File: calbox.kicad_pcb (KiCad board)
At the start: 2 copper layers, 101.6 x 76.2 mm, 80 parts, among them P1 BNC, P2 BAN+, P3 BAN-, Q1 MMBT2369, SW1 ROTARY 7POS, SW2 ROTARY 3POS, SW3 SPDT, SW4 ROTARY 12POS, SW5 DPST, U1 74LVC161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

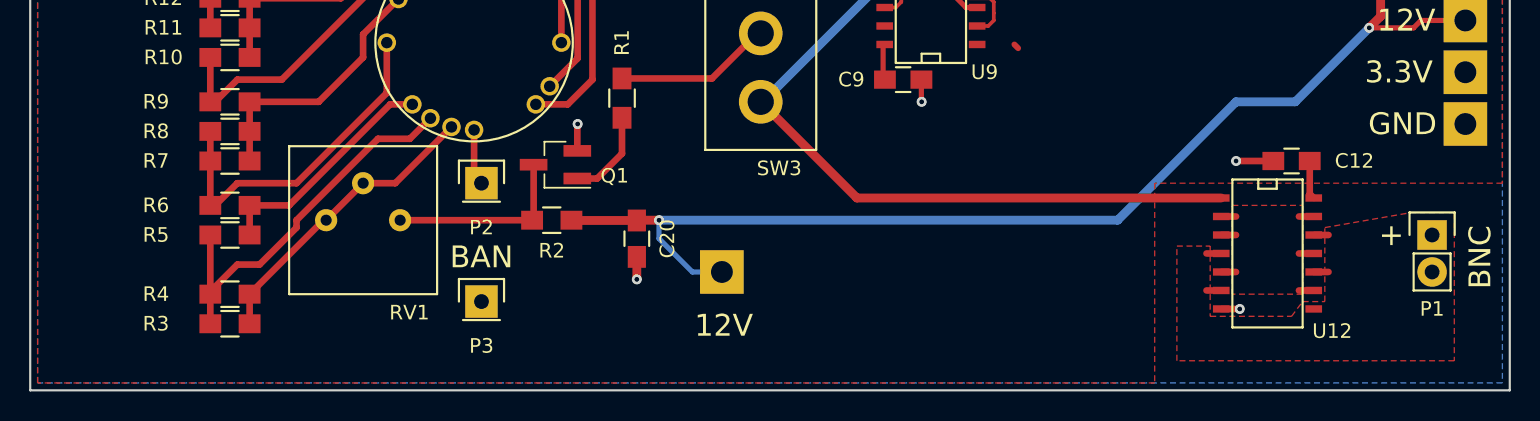
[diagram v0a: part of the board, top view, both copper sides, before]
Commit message: updated layout, specifically banana plug attachment points
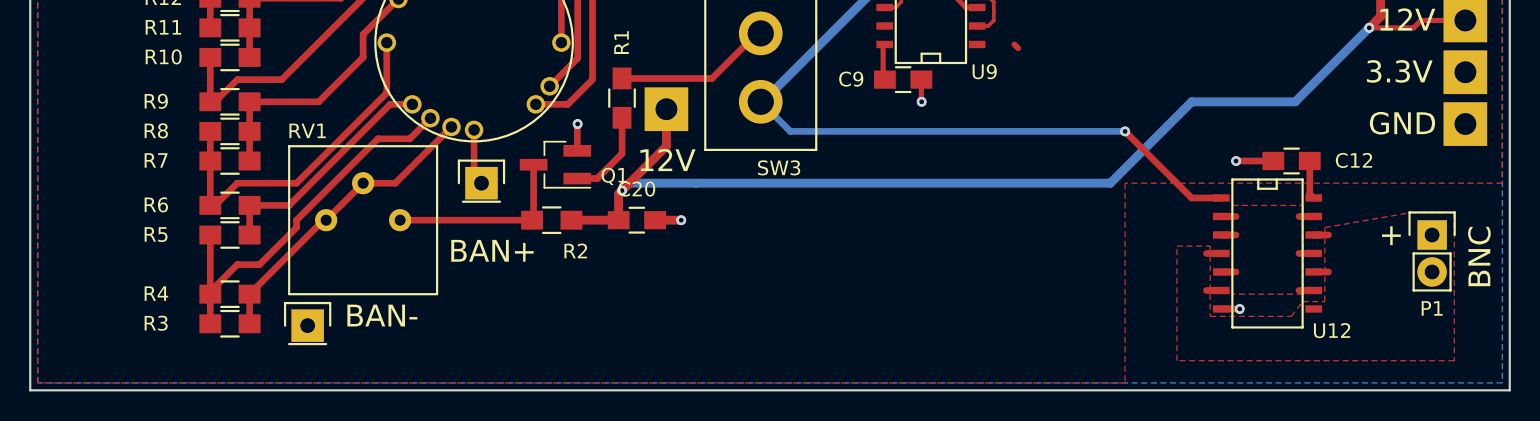
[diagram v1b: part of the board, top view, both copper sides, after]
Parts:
- moved P3 12.1 mm to (85.1, 158.1)
- moved TP1 11.8 mm to (109.7, 143.3)
- moved C20 1.27 mm to (107.7, 150.9), turned to 0 degrees
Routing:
- net +12V: track 132.9 -> 134.3 mm
- net /clock_final_division/clock_final_division_out: vias 0 -> 1
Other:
- board text added: "BAN+"
- board text added: "BAN-"
- board text removed: "BAN"

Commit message: version sent to EasyEDA 3/26/17
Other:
- board text added: "calbox Graham Keeth 3/2017"
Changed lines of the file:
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@@
     (links 255)
     (no_connects 0)
-    (area 65.964999 86.284999 167.715001 162.635001)
+    (area 31.214287 44.036 201.957715 177.96)
     (thickness 1.6)
-    (drawings 30)
-    (tracks 724)
+    (drawings 31)
+    (tracks 726)
     (zones 0)
     (modules 80)
@@
   (layers
     (0 F.Cu signal)
-    (31 B.Cu signal hide)
+    (31 B.Cu signal)
     (33 F.Adhes user)
     (35 F.Paste user)
     (37 F.SilkS user)
+    (38 B.Mask user)
     (39 F.Mask user)
-    (40 Dwgs.User user hide)
-    (41 Cmts.User user hide)
-    (42 Eco1.User user hide)
-    (43 Eco2.User user hide)
+    (40 Dwgs.User user)
+    (41 Cmts.User user)
+    (42 Eco1.User user)
+    (43 Eco2.User user)
     (44 Edge.Cuts user)
     (45 Margin user)
@@
   )
   (setup
-    (last_trace_width 0.6096)
+    (last_trace_width 0.254)
     (user_trace_width 0.3048)
     (user_trace_width 0.3556)
@@
     (visible_elements FFFEFFFF)
     (pcbplotparams
-      (layerselection 0x00030_80000001)
-      (usegerberextensions false)
+      (layerselection 0x29fe0_80000001)
+      (usegerberextensions true)
       (excludeedgelayer true)
       (linewidth 0.100000)
@@
       (plotinvisibletext false)
       (padsonsilk false)
-      (subtractmaskfromsilk false)
+      (subtractmaskfromsilk true)
       (outputformat 1)
       (mirror false)
-      (drillshape 1)
+      (drillshape 0)
       (scaleselection 1)
-      (outputdirectory ""))
+      (outputdirectory fab/gerber))
   )
   (net 0 "")
@@
     (tags "capacitor 0805")
     (attr smd)
-    (fp_text reference C20 (at 0 -2.1) (layer F.SilkS)
+    (fp_text reference C20 (at 0.254 2.159) (layer F.SilkS)
       (effects (font (size 1 1) (thickness 0.15)))
     )
@@
     )
   )
+  (gr_text "calbox\nGraham Keeth\n3/2017" (at 117.475 154.94) (layer F.SilkS)
+    (effects (font (size 1.5 1.5) (thickness 0.3) italic) (justify left))
+  )
   (gr_line (start 167.64 162.56) (end 66.04 162.56) (angle 90) (layer Edge.Cuts) (width 0.15))
   (gr_text BAN- (at 90.17 157.48) (layer F.SilkS)
@@
   (segment (start 131.064 133.731) (end 133.604 133.731) (width 0.4064) (layer F.Cu) (net 42))
   (segment (start 130.175 114.935) (end 128.69868 113.45868) (width 0.4064) (layer F.Cu) (net 42))
+  (segment (start 133.985 144.78) (end 118.237 144.78) (width 0.4572) (layer B.Cu) (net 52))
+  (segment (start 118.237 144.78) (end 116.205 142.748) (width 0.4572) (layer B.Cu) (net 52) (status 800000))
+  (segment (start 141.224 144.78) (end 133.985 144.78) (width 0.4572) (layer F.Cu) (net 52))
+  (segment (start 145.796 149.352) (end 141.224 144.78) (width 0.4572) (layer F.Cu) (net 52))
   (segment (start 147.828 149.352) (end 145.796 149.352) (width 0.4572) (layer F.Cu) (net 52))
-  (segment (start 118.237 144.78) (end 116.205 142.748) (width 0.4572) (layer B.Cu) (net 52))
-  (segment (start 141.224 144.78) (end 118.237 144.78) (width 0.4572) (layer B.Cu) (net 52))
+  (segment (start 133.985 144.78) (end 133.9215 144.7165) (width 0.4572) (layer B.Cu) (net 52))
+  (via (at 133.985 144.78) (size 0.6858) (drill 0.3302) (layers F.Cu B.Cu) (net 52))
   (segment (start 141.224 144.78) (end 141.224 144.78) (width 0.4572) (layer B.Cu) (net 52))
-  (via (at 141.224 144.78) (size 0.6858) (drill 0.3302) (layers F.Cu B.Cu) (net 52))
-  (segment (start 145.796 149.352) (end 141.224 144.78) (width 0.4572) (layer F.Cu) (net 52))
   (segment (start 116.205 142.748) (end 116.332 142.748) (width 0.6096) (layer B.Cu) (net 52))
   (segment (start 116.332 142.748) (end 133.096 125.984) (width 0.6096) (layer B.Cu) (net 52))

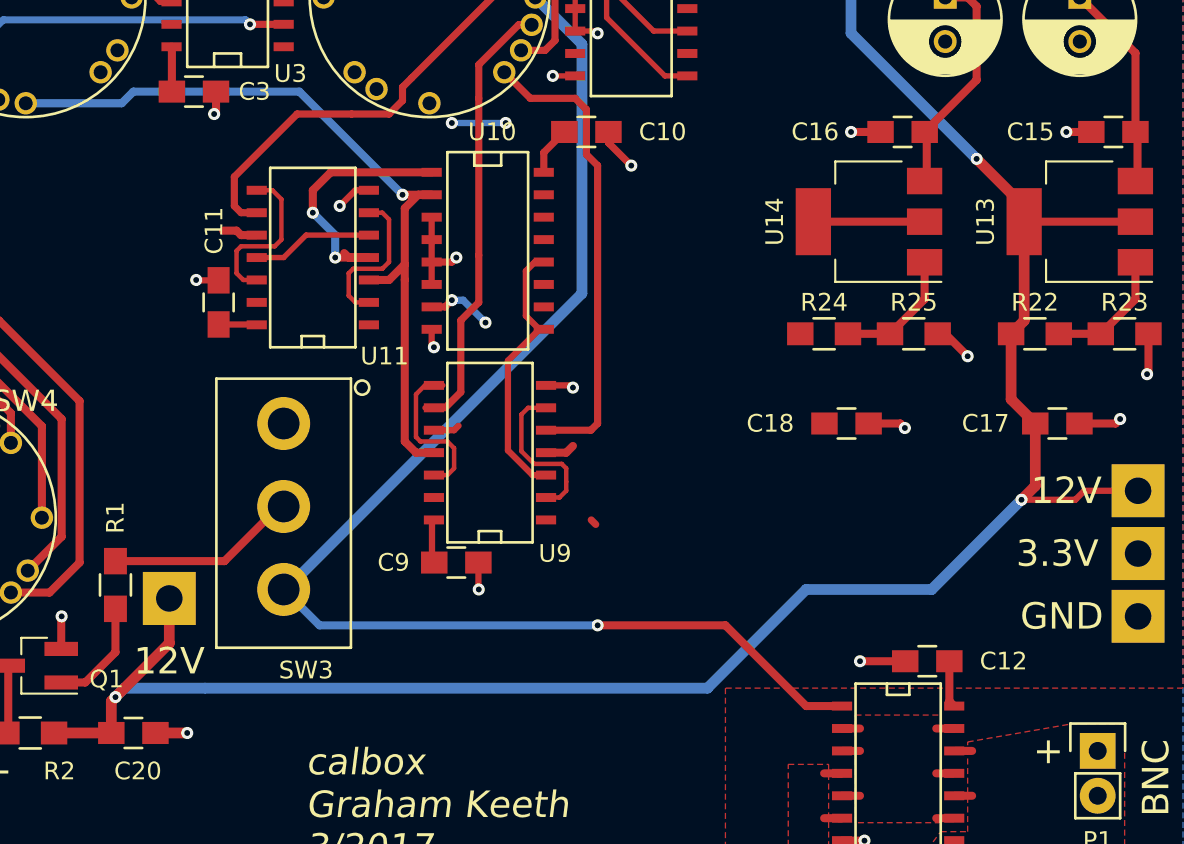
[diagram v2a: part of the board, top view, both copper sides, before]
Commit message: Several schematic & layout changes after building first boards
- increase current limiting resistors on LEDs to make them less blinding
- add speedup cap, increase base resistor on voltage output switching
  transistor for better high frequency performance (should work up to 10MHz)
- change switched/constant voltage output toggle switch to actually work
  (now toggles between switched voltage output and constant voltage
  output, rather than switched and 0V output)
- add inverter to make div-by-5 circuit work
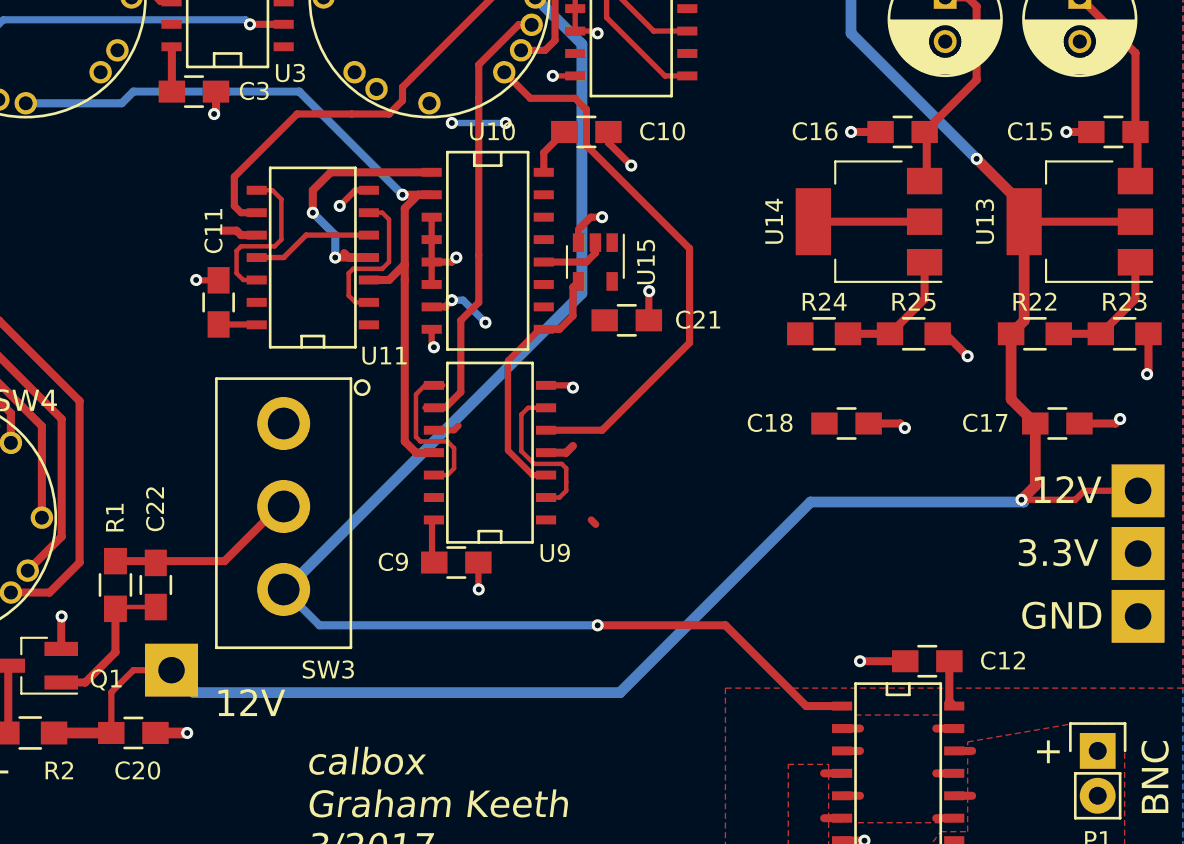
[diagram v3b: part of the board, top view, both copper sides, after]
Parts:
- added C21: 0.1u, Capacitors_SMD:C_0805_HandSoldering, F.Cu at (135.6, 127.5)
- added C22: 100p, Capacitors_SMD:C_0805_HandSoldering, F.Cu at (109.0, 142.5)
- added U15: 74LVC1G04, TO_SOT_Packages_SMD:SOT-23-5, F.Cu at (133.9, 124.2)
- R1: value 470 -> 1k
- R25: value 200 -> 196
- R27: value 5 -> 5.1
- moved TP1 4.07 mm to (109.9, 147.3)
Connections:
- SW3 pad 1: VCC -> GND
- U10 pad 12: /clock_final_division/div_by_5 -> Net-(U10-Pad12)
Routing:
- net +12V: track 134.3 -> 129.0 mm, vias 3 -> 2
- net /clock_final_division/div_by_5_out: track 26.6 -> 31.3 mm
- net GND: track 104.8 -> 108.8 mm, vias 44 -> 46
- net Net-(U10-Pad12): track 0.00 -> 3.72 mm
- net Net-(C22-Pad1): track 6.24 -> 8.57 mm
- net /clock_final_division/div_by_5: track 15.4 -> 14.6 mm

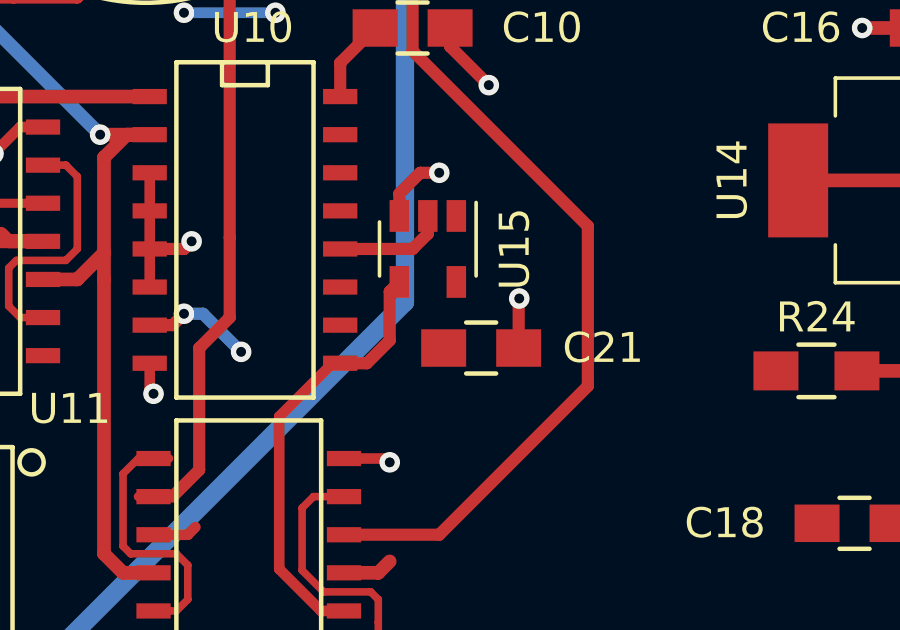
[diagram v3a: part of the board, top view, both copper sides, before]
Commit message: update layout for div-by-5 inverter
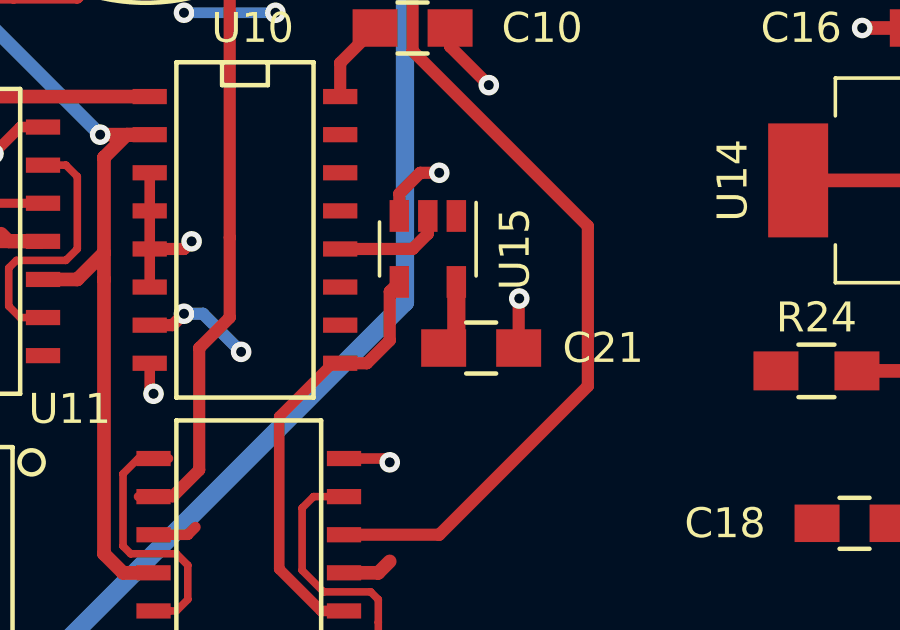
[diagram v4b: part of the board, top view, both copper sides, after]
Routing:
- net VCC: track 92.9 -> 95.2 mm
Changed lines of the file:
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@@
     (thickness 1.6)
     (drawings 31)
-    (tracks 737)
+    (tracks 739)
     (zones 0)
     (modules 83)
@@
   (layers
     (0 F.Cu signal)
-    (31 B.Cu signal)
+    (31 B.Cu signal hide)
     (33 F.Adhes user)
     (35 F.Paste user)
@@
   (segment (start 69.85 95.23) (end 69.85 97.155) (width 0.3556) (layer F.Cu) (net 3))
   (via (at 69.85 97.155) (size 0.6858) (drill 0.3302) (layers F.Cu B.Cu) (net 3))
+  (segment (start 134.808 125.306) (end 134.808 127.086) (width 0.6096) (layer F.Cu) (net 4) (status C00000))
+  (segment (start 134.808 127.086) (end 134.386 127.508) (width 0.6096) (layer F.Cu) (net 4) (status C00000))
   (segment (start 124.587 119.126) (end 118.872 119.126) (width 0.4572) (layer F.Cu) (net 4))
   (segment (start 118.872 119.126) (end 117.856 120.142) (width 0.4572) (layer F.Cu) (net 4))
@@
   (segment (start 158.115 137.668) (end 157.988 137.668) (width 0.6096) (layer F.Cu) (net 7))
   (via (at 157.988 137.668) (size 0.6858) (drill 0.3302) (layers F.Cu B.Cu) (net 7))
-  (segment (start 135.255 148.59) (end 111.125 148.59) (width 0.6096) (layer B.Cu) (net 7) (status 800000))
+  (segment (start 135.255 148.59) (end 111.125 148.59) (width 0.6096) (layer B.Cu) (net 7))
   (segment (start 146.05 137.795) (end 135.255 148.59) (width 0.6096) (layer B.Cu) (net 7))
   (segment (start 158.115 137.795) (end 146.05 137.795) (width 0.6096) (layer B.Cu) (net 7))
   (segment (start 157.988 137.668) (end 158.115 137.795) (width 0.6096) (layer B.Cu) (net 7))
-  (segment (start 111.125 148.59) (end 109.855 147.32) (width 0.6096) (layer B.Cu) (net 7) (status C00000))
+  (segment (start 111.125 148.59) (end 109.855 147.32) (width 0.6096) (layer B.Cu) (net 7))
   (segment (start 106.446 150.876) (end 106.446 148.57) (width 0.3556) (layer F.Cu) (net 7))
   (segment (start 106.446 148.57) (end 107.696 147.32) (width 0.3556) (layer F.Cu) (net 7))

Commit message: Layout changes for r1
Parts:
- BT1, BT2: footprint Pin_Headers:Pin_Header_Straight_1x02 -> calbox:battery_snap
- moved BT1 1.80 mm to (162.6, 92.1)
- moved BT2 1.27 mm to (162.6, 99.7)
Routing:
- net Net-(BT1-Pad2): track 20.2 -> 17.7 mm
- net Net-(BT1-Pad1): track 9.83 -> 8.16 mm
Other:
- board text added: "calbox r1 Graham Keeth 5/2017"
- board text removed: "calbox Graham Keeth 3/2017"
